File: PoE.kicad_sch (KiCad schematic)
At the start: 40 parts, among them J1001 8P8C_LED_Shielded_x2, J1002 8P8C_LED_Shielded_x2, U1001 7490220122, U1002 TCMT1107

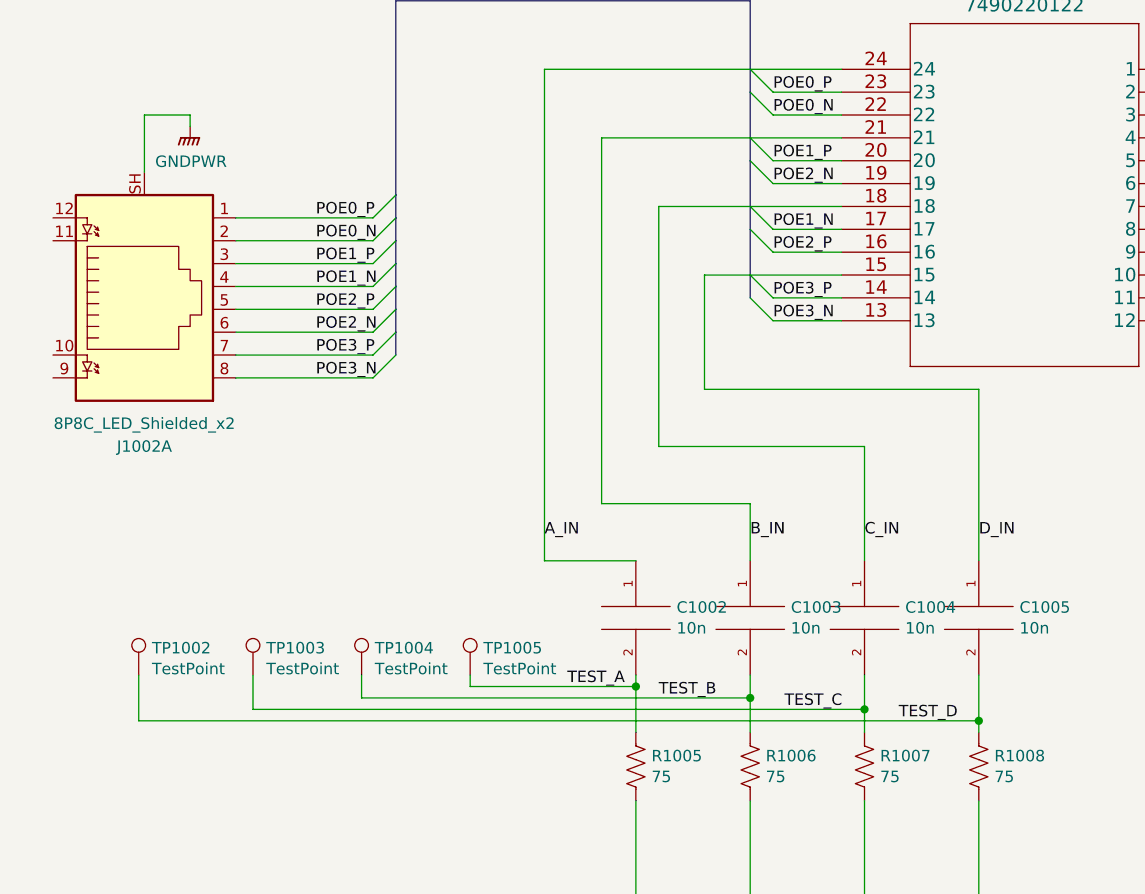
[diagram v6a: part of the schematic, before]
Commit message: Redoing ethernet routing
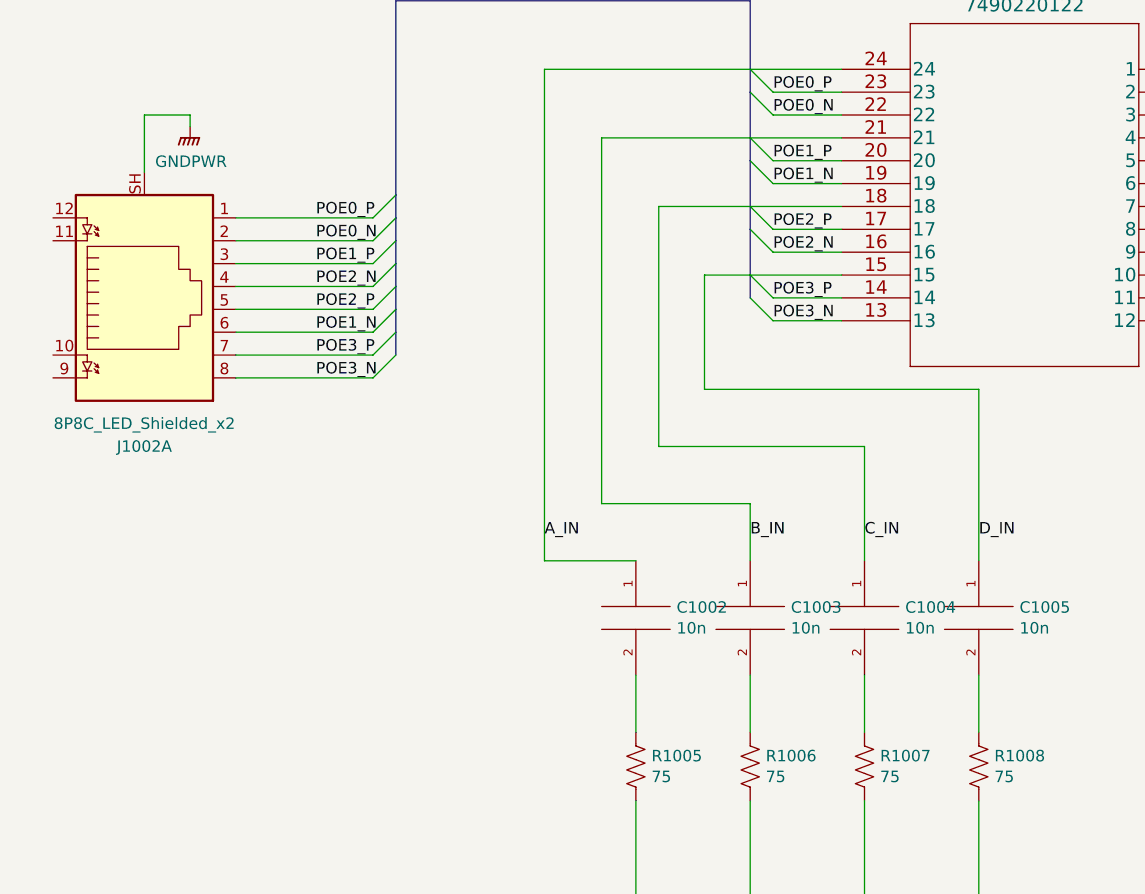
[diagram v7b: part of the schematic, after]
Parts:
- removed TP1002, TP1003, TP1004, TP1005: TestPoint, SparkFun-Connector:TestPoint-1.0mm, symbol Connector:TestPoint
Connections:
- net POE1_N: now also J1002.6, U1001.19; no longer J1002.4, U1001.17
- net POE2_N: now also J1002.4, U1001.16; no longer J1002.6, U1001.19
- net POE2_P: now also U1001.17; no longer U1001.16
- net TEST_A: no longer names the net of C1002.2, R1005.1
- net TEST_B: no longer names the net of C1003.2, R1006.1
- net TEST_C: no longer names the net of C1004.2, R1007.1
- net TEST_D: no longer names the net of C1005.2, R1008.1

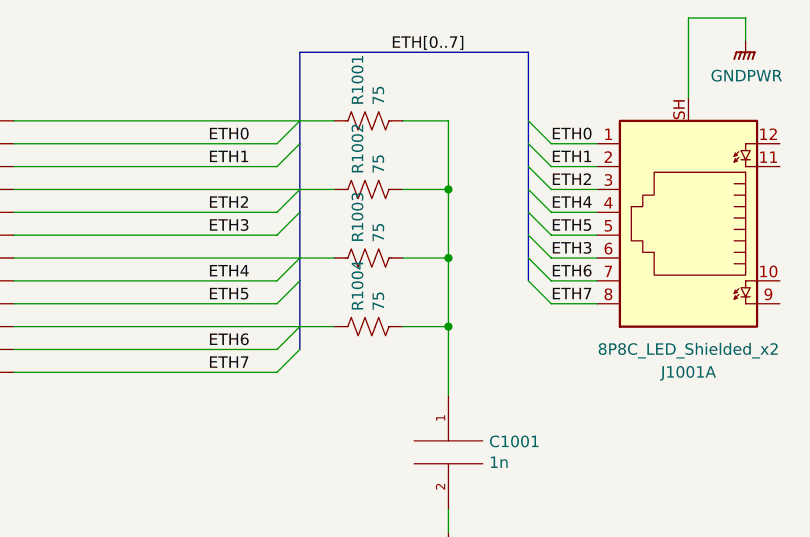
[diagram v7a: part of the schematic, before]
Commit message: Routing updates to ethernet
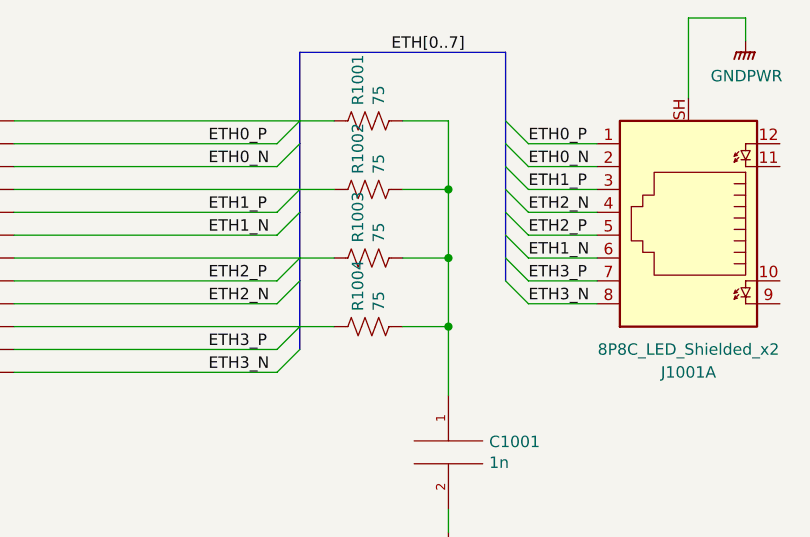
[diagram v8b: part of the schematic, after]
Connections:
- net ETH0 renamed ETH0_P
- net ETH1 renamed ETH0_N
- net ETH2 renamed ETH1_P
- net ETH3 renamed ETH1_N
- net ETH4 renamed ETH2_N
- net ETH2_N: now also U1001.9; no longer U1001.8
- net ETH5 renamed ETH2_P
- net ETH2_P: now also U1001.8; no longer U1001.9
- net ETH6 renamed ETH3_P
- net ETH7 renamed ETH3_N
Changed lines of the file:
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@@
 	)
 	(bus_entry
-		(at 215.9 45.72)
+		(at 213.36 45.72)
 		(size 2.54 2.54)
 		(stroke
@@
 	)
 	(bus_entry
-		(at 215.9 38.1)
+		(at 213.36 38.1)
 		(size 2.54 2.54)
 		(stroke
@@
 	)
 	(bus_entry
-		(at 215.9 43.18)
+		(at 213.36 43.18)
 		(size 2.54 2.54)
 		(stroke
@@
 	)
 	(bus_entry
-		(at 215.9 30.48)
+		(at 213.36 30.48)
 		(size 2.54 2.54)
 		(stroke
@@
 	)
 	(bus_entry
-		(at 215.9 33.02)
+		(at 213.36 33.02)
 		(size 2.54 2.54)
 		(stroke
@@
 	)
 	(bus_entry
-		(at 215.9 35.56)
+		(at 213.36 35.56)
 		(size 2.54 2.54)
 		(stroke
@@
 	)
 	(bus_entry
-		(at 215.9 40.64)
+		(at 213.36 40.64)
 		(size 2.54 2.54)
 		(stroke
@@
 	)
 	(bus_entry
-		(at 215.9 27.94)
+		(at 213.36 27.94)
 		(size 2.54 2.54)
 		(stroke
@@
 	(bus
 		(pts
-			(xy 215.9 43.18) (xy 215.9 45.72)
+			(xy 213.36 43.18) (xy 213.36 45.72)
 		)
 		(stroke
@@
 	(bus
 		(pts
-			(xy 215.9 20.32) (xy 215.9 27.94)
-		)
-		(stroke
-			(width 0)
-			(type default)
-		)
-	)
-	(bus
-		(pts
-			(xy 215.9 40.64) (xy 215.9 43.18)
+			(xy 213.36 20.32) (xy 213.36 27.94)
+		)
+		(stroke
+			(width 0)
+			(type default)
+		)
+	)
+	(bus
+		(pts
+			(xy 213.36 40.64) (xy 213.36 43.18)
 		)
 		(stroke
@@
 	(bus
 		(pts
-			(xy 190.5 20.32) (xy 215.9 20.32)
-		)
-		(stroke
-			(width 0)
-			(type default)
-		)
-	)
-	(wire
-		(pts
-			(xy 218.44 38.1) (xy 223.52 38.1)
+			(xy 190.5 20.32) (xy 213.36 20.32)
+		)
+		(stroke
+			(width 0)
+			(type default)
+		)
+	)
+	(wire
+		(pts
+			(xy 215.9 38.1) (xy 223.52 38.1)
 		)
 		(stroke
@@
 	(bus
 		(pts
-			(xy 215.9 30.48) (xy 215.9 33.02)
+			(xy 213.36 30.48) (xy 213.36 33.02)
 		)
 		(stroke
@@
 	(wire
 		(pts
-			(xy 218.44 43.18) (xy 223.52 43.18)
+			(xy 215.9 43.18) (xy 223.52 43.18)
 		)
 		(stroke
@@
 	(wire
 		(pts
-			(xy 218.44 33.02) (xy 223.52 33.02)
+			(xy 215.9 33.02) (xy 223.52 33.02)
 		)
 		(stroke
@@
 	(wire
 		(pts
-			(xy 218.44 45.72) (xy 223.52 45.72)
+			(xy 215.9 45.72) (xy 223.52 45.72)
 		)
 		(stroke
@@
 	(bus
 		(pts
-			(xy 215.9 38.1) (xy 215.9 40.64)
+			(xy 213.36 38.1) (xy 213.36 40.64)
 		)
 		(stroke
@@
 	(wire
 		(pts
-			(xy 218.44 40.64) (xy 223.52 40.64)
+			(xy 215.9 40.64) (xy 223.52 40.64)
 		)
 		(stroke
@@
 	(wire
 		(pts
-			(xy 218.44 35.56) (xy 223.52 35.56)
+			(xy 215.9 35.56) (xy 223.52 35.56)
 		)
 		(stroke
@@
 	(bus
 		(pts
-			(xy 215.9 27.94) (xy 215.9 30.48)
+			(xy 213.36 27.94) (xy 213.36 30.48)
 		)
 		(stroke
@@
 	(wire
 		(pts
-			(xy 218.44 48.26) (xy 223.52 48.26)
-		)
-		(stroke
-			(width 0)
-			(type default)
-		)
-	)
-	(wire
-		(pts
-			(xy 223.52 30.48) (xy 218.44 30.48)
+			(xy 215.9 48.26) (xy 223.52 48.26)
+		)
+		(stroke
+			(width 0)
+			(type default)
+		)
+	)
+	(wire
+		(pts
+			(xy 215.9 30.48) (xy 223.52 30.48)
 		)
 		(stroke
@@
 	(bus
 		(pts
-			(xy 215.9 35.56) (xy 215.9 38.1)
-		)
-		(stroke
-			(width 0)
-			(type default)
-		)
-	)
-	(bus
-		(pts
-			(xy 215.9 33.02) (xy 215.9 35.56)
+			(xy 213.36 35.56) (xy 213.36 38.1)
+		)
+		(stroke
+			(width 0)
+			(type default)
+		)
+	)
+	(bus
+		(pts
+			(xy 213.36 33.02) (xy 213.36 35.56)
 		)
 		(stroke
@@
 		)
 	)
-	(label "ETH6"
-		(at 218.44 45.72 0)
+	(label "ETH3_P"
+		(at 215.9 45.72 0)
 		(fields_autoplaced yes)
 		(effects
@@
 		)
 	)
-	(label "ETH2"
-		(at 218.44 35.56 0)
+	(label "ETH1_P"
+		(at 215.9 35.56 0)
 		(fields_autoplaced yes)
 		(effects
@@
 		)
 	)
-	(label "ETH4"
-		(at 218.44 38.1 0)
+	(label "ETH2_N"
+		(at 215.9 38.1 0)
 		(fields_autoplaced yes)
 		(effects
@@
 		)
 	)
-	(label "ETH5"
-		(at 218.44 40.64 0)
+	(label "ETH2_P"
+		(at 215.9 40.64 0)
 		(fields_autoplaced yes)
 		(effects
@@
 		)
 	)
-	(label "ETH7"
+	(label "ETH3_N"
 		(at 180.34 55.88 0)
 		(fields_autoplaced yes)
@@
 		)
 	)
-	(label "ETH3"
+	(label "ETH1_N"
 		(at 180.34 40.64 0)
 		(fields_autoplaced yes)
@@
 		)
 	)
-	(label "ETH5"
+	(label "ETH2_N"
 		(at 180.34 48.26 0)
 		(fields_autoplaced yes)
@@
 		)
 	)
-	(label "ETH4"
+	(label "ETH2_P"
 		(at 180.34 45.72 0)
 		(fields_autoplaced yes)
@@
 		)
 	)
-	(label "ETH2"
+	(label "ETH1_P"
 		(at 180.34 38.1 0)
 		(fields_autoplaced yes)
@@
 		)
 	)
-	(label "ETH0"
+	(label "ETH0_P"
 		(at 180.34 30.48 0)
 		(fields_autoplaced yes)
@@
 		)
 	)
-	(label "ETH6"
+	(label "ETH3_P"
 		(at 180.34 53.34 0)
 		(fields_autoplaced yes)
@@
 		)
 	)
-	(label "ETH1"
+	(label "ETH0_N"
 		(at 180.34 33.02 0)
 		(fields_autoplaced yes)
@@
 		)
 	)
-	(label "ETH7"
-		(at 218.44 48.26 0)
-		(fields_autoplaced yes)
-		(effects
-			(font
-				(size 1.27 1.27)
-			)
-			(justify left bottom)
-		)
-	)
-	(label "ETH1"
-		(at 218.44 33.02 0)
-		(fields_autoplaced yes)
-		(effects
-			(font
-				(size 1.27 1.27)
-			)
-			(justify left bottom)
-		)
-	)
-	(label "ETH3"
-		(at 218.44 43.18 0)
+	(label "ETH3_N"
+		(at 215.9 48.26 0)
+		(fields_autoplaced yes)
+		(effects
+			(font
+				(size 1.27 1.27)
+			)
+			(justify left bottom)
+		)
+	)
+	(label "ETH0_N"
+		(at 215.9 33.02 0)
+		(fields_autoplaced yes)
+		(effects
+			(font
+				(size 1.27 1.27)
+			)
+			(justify left bottom)
+		)
+	)
+	(label "ETH1_N"
+		(at 215.9 43.18 0)
 		(fields_autoplaced yes)
 		(effects
@@
 		)
 	)
-	(label "ETH0"
-		(at 218.44 30.48 0)
-		(fields_autoplaced yes)
-		(effects
+	(label "ETH0_P"
+		(at 215.9 30.48 0)
+		(fields_autoplaced yes)
+		(effects
